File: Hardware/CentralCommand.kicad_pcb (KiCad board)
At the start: 4 copper layers, 56 parts, among them IC101 STM32F030C8, IC201 FT232RQ, P101 I2C, P102 GPIO1, P103 GPIO1, P104 USART, P105 SPI, P106 ADC, P201 USB_OTG, P202 POWER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

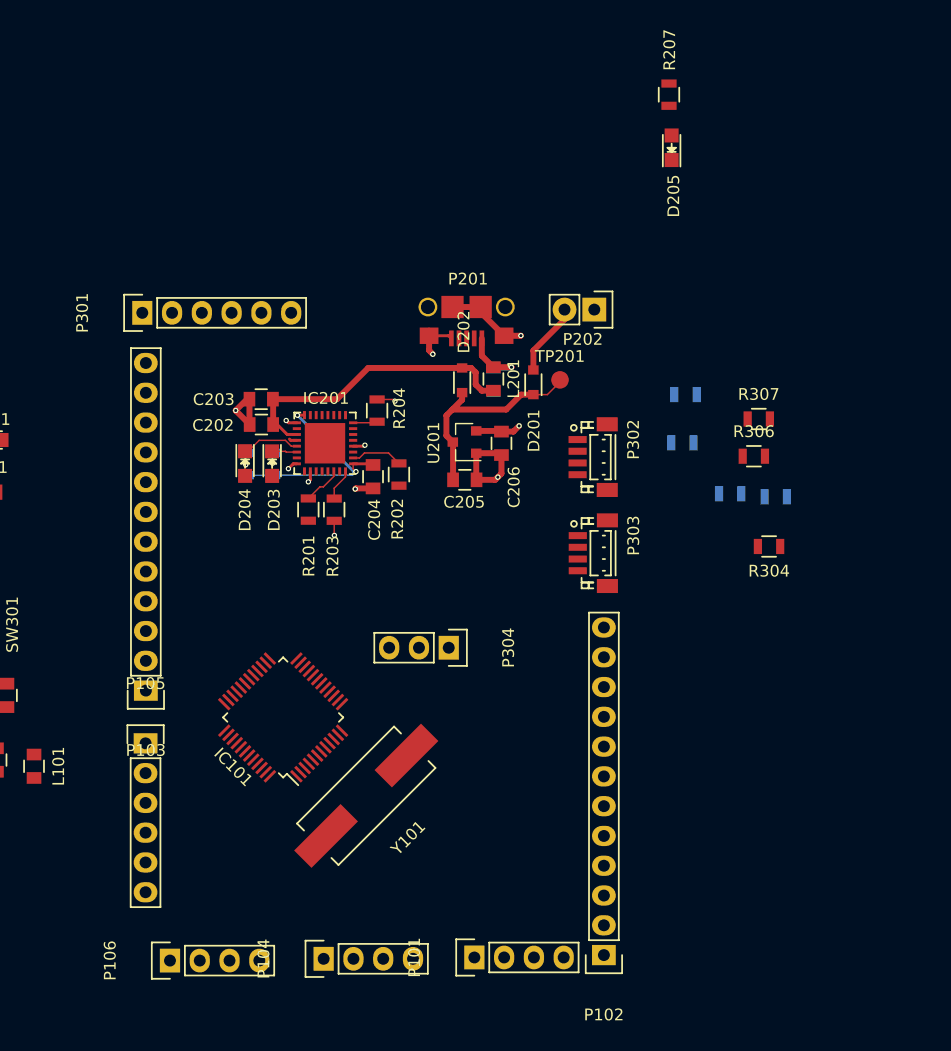
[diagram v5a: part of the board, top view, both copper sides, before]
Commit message: moved headers from power side of boards and rerouted traces
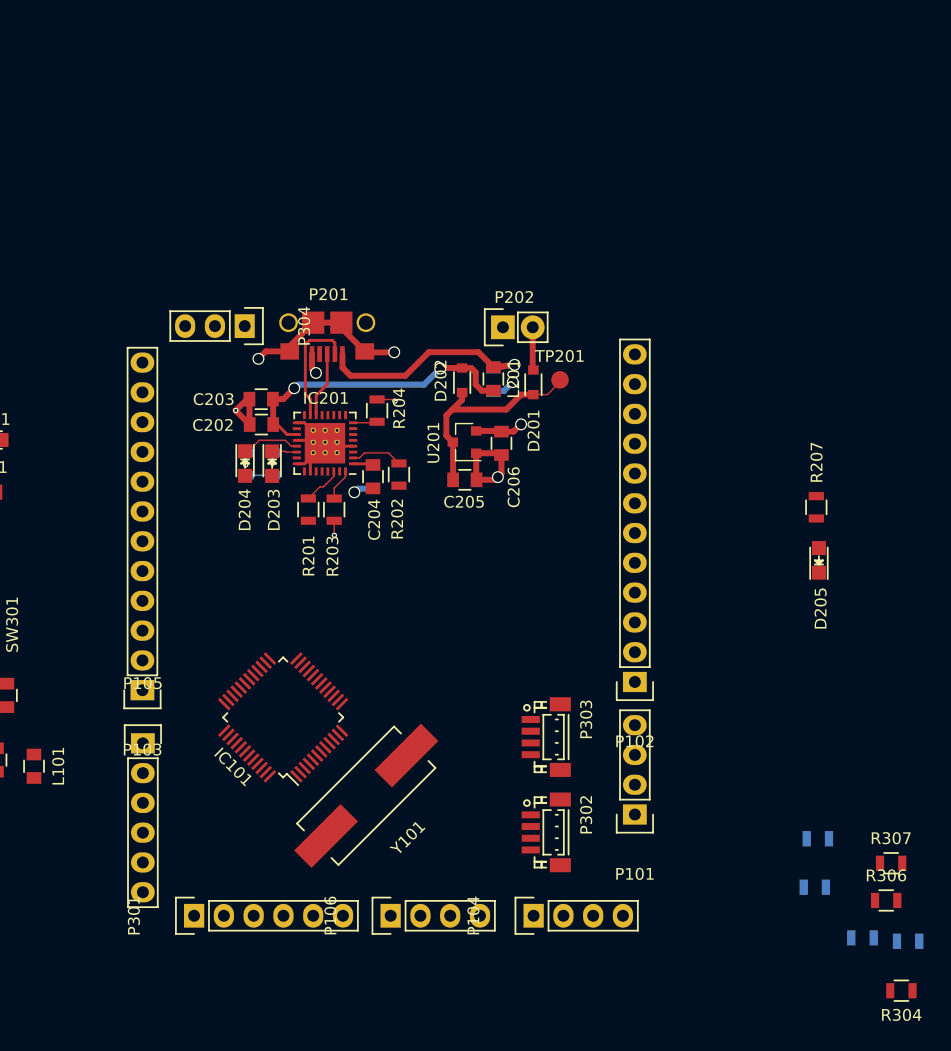
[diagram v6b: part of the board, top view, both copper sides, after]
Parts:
- added REF**: via, CentralCommand:via, F.Cu at (122.9, 78.9)
- added REF**: via, CentralCommand:via, F.Cu at (124.0, 78.9)
- added REF**: via, CentralCommand:via, F.Cu at (125.0, 78.9)
- added REF**: via, CentralCommand:via, F.Cu at (125.0, 78.0)
- added REF**: via, CentralCommand:via, F.Cu at (124.0, 78.0)
- added REF**: via, CentralCommand:via, F.Cu at (122.9, 78.0)
- added REF**: via, CentralCommand:via, F.Cu at (125.0, 77.0)
- added REF**: via, CentralCommand:via, F.Cu at (124.0, 77.0)
- added REF**: via, CentralCommand:via, F.Cu at (122.9, 77.0)
- IC201: footprint Housings_DFN_QFN:QFN-32-1EP_5x5mm_Pitch0.5mm -> CentralCommand:FT232RQ
- moved P301 51.6 mm to (112.8, 118.4)
- moved R305 39.5 mm to (165.7, 115.9)
- moved R301 39.5 mm to (173.7, 120.5)
- moved R302 39.5 mm to (169.8, 120.3)
- moved R303 39.5 mm to (166.0, 111.8)
- moved R304 39.5 mm to (173.1, 124.8)
- moved R306 39.5 mm to (171.8, 117.1)
- moved R307 39.5 mm to (172.2, 113.9)
- moved D205 37.4 mm to (166.1, 88.1)
- moved R207 37.4 mm to (165.8, 83.5)
- moved P304 32.5 mm to (117.1, 68.1)
- moved P302 32.3 mm to (142.7, 111.3)
- moved P102 23.4 mm to (150.4, 98.4)
- moved P106 19.2 mm to (129.5, 118.4)
- moved P101 18.3 mm to (150.4, 109.7), turned to 180 degrees
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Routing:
- net Net-(C204-Pad1): track 19.6 -> 4.01 mm, vias 2 -> 0
- net GND: track 34.0 -> 48.8 mm, vias 11 -> 8
- net Net-(C201-Pad1): track 5.96 -> 19.3 mm
- net Net-(IC201-Pad15): track 0.00 -> 9.90 mm
- net Net-(IC201-Pad14): track 0.00 -> 5.60 mm
- net Net-(D201-Pad2): track 6.25 -> 3.67 mm
- net (no net): track 0.00 -> 1.70 mm, vias 0 -> 1
- net Net-(C202-Pad1): vias 0 -> 2
- added copper zone on PWR, net /PWR

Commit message: continued pcb layout
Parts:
- R207: moved to B.Cu
- moved SW301 43.2 mm to (136.5, 86.9)
- moved C301 42.2 mm to (136.6, 87.0)
- moved D205 38.5 mm to (133.2, 67.8), turned to 180 degrees
- moved R207 36.2 mm to (133.2, 67.8), turned to 0 degrees
- moved P101 35.3 mm to (116.2, 118.6), turned to 270 degrees
- moved P104 34.4 mm to (108.1, 110.8), turned to 180 degrees
- moved P103 28.9 mm to (108.1, 70.2), turned to 0 degrees
- moved P105 28.5 mm to (132.8, 118.4), turned to 270 degrees
- moved P301 23.8 mm to (136.6, 118.4)
- moved P106 22.6 mm to (150.4, 109.7), turned to 180 degrees
- moved D101 19.5 mm to (102.9, 95.7)
- moved R101 12.3 mm to (102.7, 92.0)
- moved R304 11.8 mm to (171.8, 113.1), turned to 0 degrees
- moved R303 11.0 mm to (175.5, 106.3), turned to 180 degrees
- moved R301 10.4 mm to (175.4, 110.3)
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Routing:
- net /NRST: track 0.00 -> 34.0 mm, vias 0 -> 2
- net Net-(C204-Pad1): track 4.01 -> 26.3 mm, vias 0 -> 2
- net GND: track 48.8 -> 59.9 mm, vias 8 -> 11
- net Net-(D205-Pad2): track 0.00 -> 2.88 mm, vias 0 -> 1
- net Net-(D204-Pad2): track 1.99 -> 4.07 mm
- net (no net): track 1.70 -> 0.27 mm, vias 1 -> 0
- net /PWR: track 4.09 -> 5.49 mm, vias 1 -> 2
- net Net-(D203-Pad2): track 1.99 -> 3.15 mm

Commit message: more layout
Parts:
- C101, C102, C103, C104, C105, C106, C107, C108, L101, R101, R304, R306, R307: moved to B.Cu
- R301: moved to F.Cu
- moved C101 45.7 mm to (130.6, 105.1), turned to 225 degrees
- moved D101 44.1 mm to (143.2, 77.7), turned to 90 degrees
- moved R101 43.0 mm to (143.3, 77.8), turned to 90 degrees
- moved R301 39.1 mm to (136.5, 114.8), turned to 90 degrees
- moved C104 38.3 mm to (122.0, 109.3), turned to 225 degrees
- moved C102 36.8 mm to (125.0, 110.6), turned to 45 degrees
- moved R302 33.7 mm to (143.5, 106.6)
- moved R303 32.1 mm to (143.5, 108.7), turned to 0 degrees
- moved R305 31.9 mm to (143.5, 113.0)
- moved C106 31.0 mm to (122.2, 97.7), turned to 315 degrees
- moved R306 30.8 mm to (142.4, 101.6), turned to 180 degrees
- moved R307 30.2 mm to (142.3, 99.5), turned to 180 degrees
- moved C107 29.8 mm to (118.4, 99.8), turned to 225 degrees
- moved R304 28.4 mm to (143.5, 110.8)
- moved C103 27.7 mm to (119.1, 94.2), turned to 135 degrees
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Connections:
- P102 pad 11: /MCO -> /PB2
- P102 pad 12: /PA11 -> /PB10
- P103 pad 10: /PB13 -> /MCO
- P103 pad 11: /PB14 -> /PA11
- P103 pad 12: /PB15 -> /PA12
- P103 pad 3: /PA12 -> /PB11
- P103 pad 4: /PB2 -> /PB12
- P103 pad 5: /PB8 -> /PB13
- P103 pad 6: /PB9 -> /PB14
- P103 pad 7: /PB10 -> /PB15
- P103 pad 8: /PB11 -> /PB8
- P103 pad 9: /PB12 -> /PB9
- R101 pad 1: /PB15 -> /PB10
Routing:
- net /NRST: track 34.0 -> 90.5 mm, vias 2 -> 7
- net /SWDIO: track 0.00 -> 49.9 mm, vias 0 -> 1
- net /PB10: track 0.00 -> 44.9 mm, vias 0 -> 1
- net /PB2: track 0.00 -> 43.7 mm
- net /I2C1_SCL: track 0.00 -> 43.6 mm, vias 0 -> 3
- net /BOOT0: track 0.00 -> 41.8 mm, vias 0 -> 2
- net /PA7: track 0.00 -> 40.9 mm
- net /PA6: track 0.00 -> 38.6 mm
- net /I2C1_SDA: track 0.00 -> 38.3 mm, vias 0 -> 3
- net /ADC_IN8: track 0.00 -> 38.0 mm, vias 0 -> 2
- net /SWCLK: track 0.00 -> 37.9 mm, vias 0 -> 1
- net /ADC_IN9: track 0.00 -> 37.2 mm, vias 0 -> 2
- net /PA5: track 0.00 -> 37.1 mm
- net /PA0: track 0.00 -> 35.9 mm
- net /PA4: track 0.00 -> 35.9 mm
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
